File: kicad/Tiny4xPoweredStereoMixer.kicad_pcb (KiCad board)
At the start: 4 copper layers, 99.1 x 56.5 mm, 54 parts, among them J1 RCJ-2221, J2 RCJ-2221, J3 RCJ-2221, J4 RCJ-2221, J5 RCJ-2221, J6 PowerConnector, J7 PowerConnector, J8 PowerConnector, U1 TL072, U2 TL072, U3 TL072, U4 TL072, U5 TL072, U6 LM2611AMF/NOPB

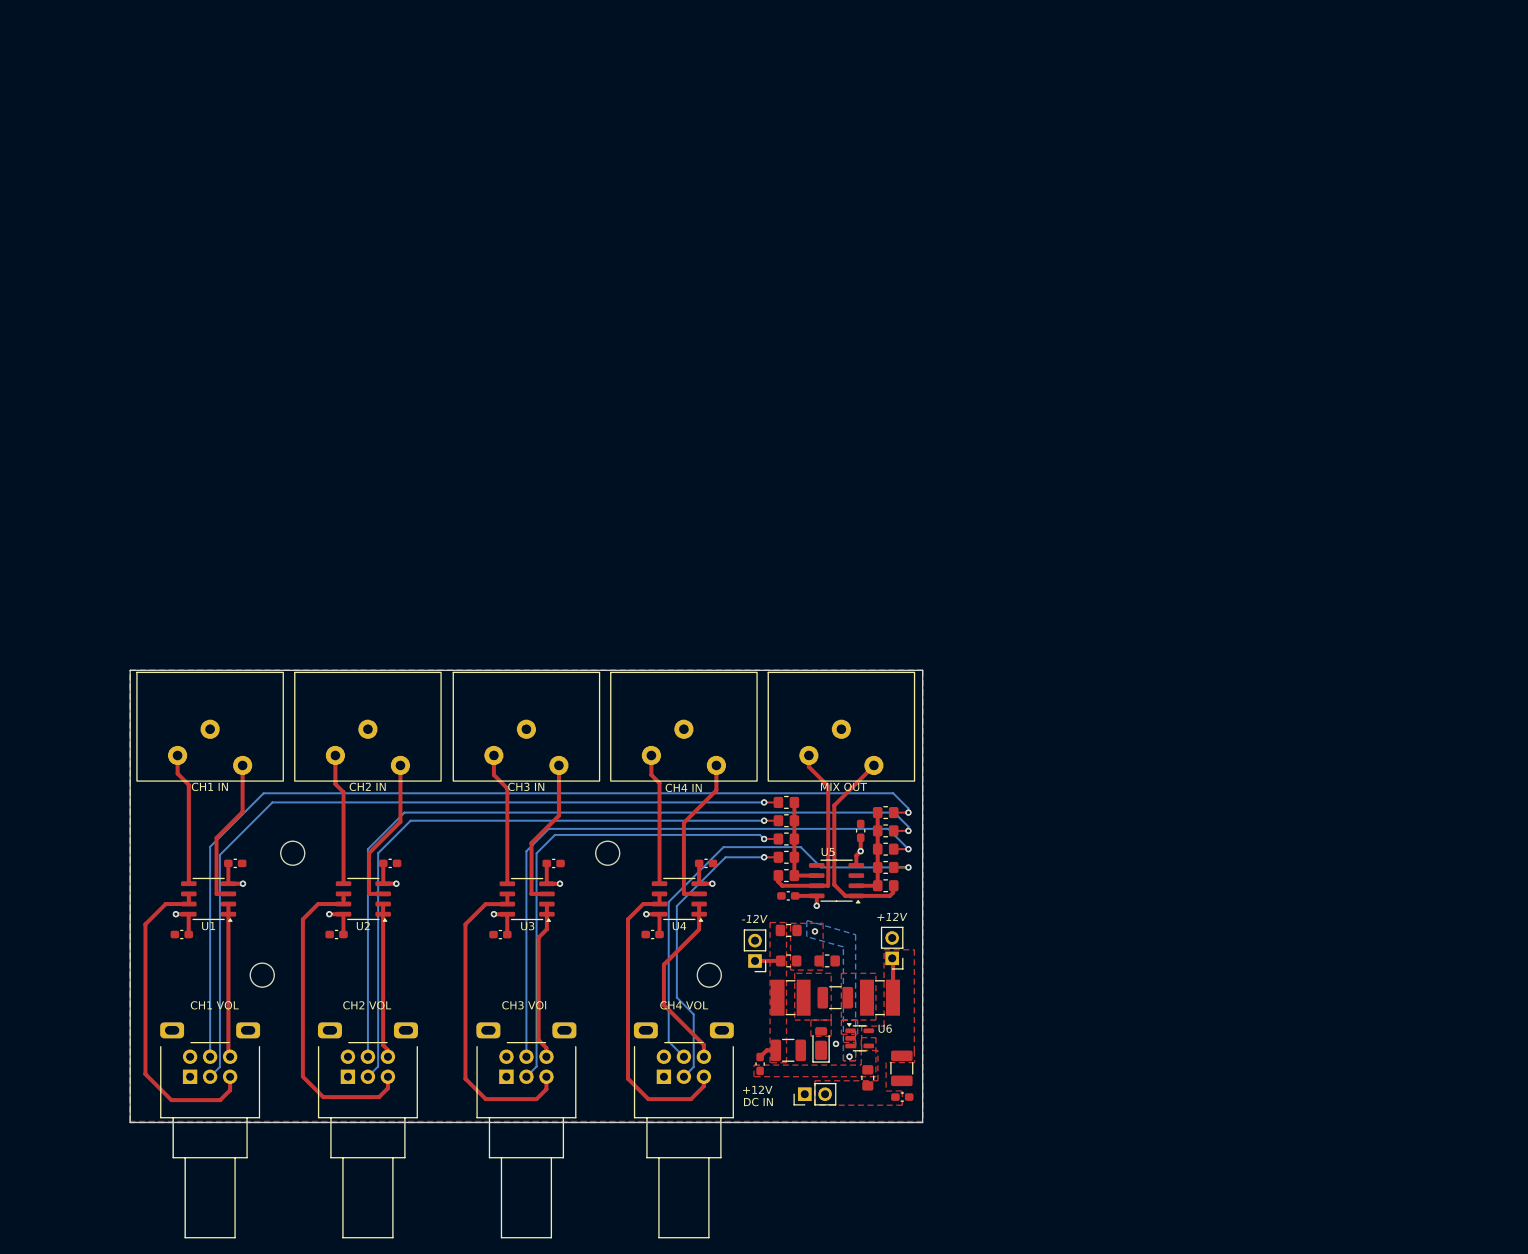
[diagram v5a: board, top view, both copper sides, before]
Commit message: - updated pots to rk12l12
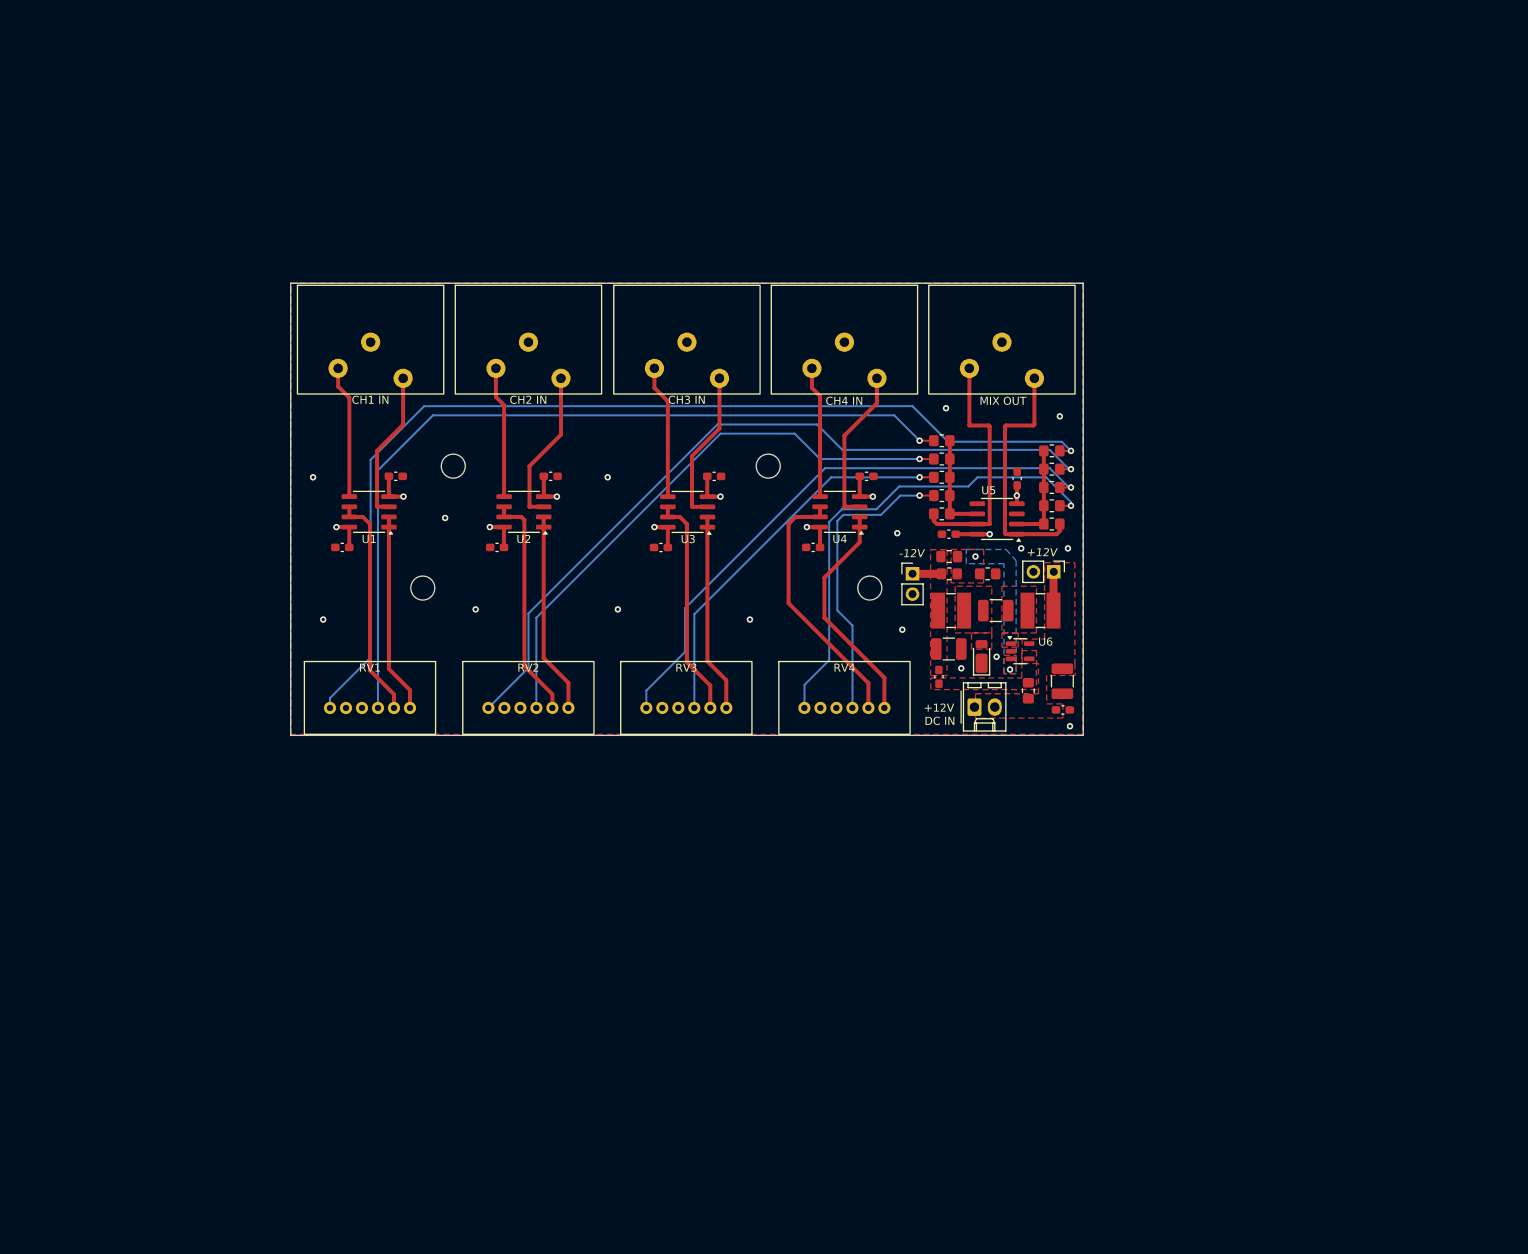
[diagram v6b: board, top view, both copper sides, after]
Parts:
- J6: footprint Connector_PinHeader_2.54mm:PinHeader_1x02_P2.54mm_Vertical -> Connector_Molex:Molex_KK-254_AE-6410-02A_1x02_P2.54mm_Vertical
- RV1, RV2, RV3, RV4: footprint Potentiometers:Potentiometer_Alps_RK09L_Double_Horizontal -> Potentiometers:Alps_RK12L12_Double_Horizontal
- moved RV4 54.3 mm to (173.1, 100.5), turned to 0 degrees
- moved RV2 54.3 mm to (133.6, 100.5), turned to 0 degrees
- moved RV3 54.3 mm to (153.3, 100.5), turned to 0 degrees
- moved RV1 54.3 mm to (113.8, 100.5), turned to 0 degrees
- moved C4 54.0 mm to (186.1, 96.4)
- moved C16 53.3 mm to (184.9, 99.9)
- moved J6 52.8 mm to (189.4, 103.7), turned to 0 degrees
- moved C11 52.4 mm to (150.2, 83.7)
- moved C13 52.4 mm to (169.2, 83.7)
- moved C5 52.4 mm to (129.7, 83.7)
- moved U6 52.4 mm to (195.1, 96.7)
- moved C7 52.4 mm to (110.3, 83.7)
- moved C1 52.4 mm to (200.3, 100.4)
- moved C12 52.4 mm to (156.8, 74.8)
- moved C14 52.4 mm to (175.9, 74.8)
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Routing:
- net Net-(U1B--): track 40.6 -> 28.4 mm
- net Net-(U3B--): track 40.1 -> 28.2 mm
- net Net-(U2B--): track 40.4 -> 28.9 mm
- net /ch3_right_mix_in: track 59.8 -> 48.7 mm
- net /ch2_right_mix_in: track 80.2 -> 71.8 mm
- net /ch1_left_mix_in: track 119.4 -> 127.2 mm
- net Net-(U4A--): track 23.0 -> 28.8 mm
- net Net-(U2A--): track 19.3 -> 25.2 mm
- net Net-(U1A--): track 19.2 -> 25.0 mm
- net Net-(U4B--): track 38.3 -> 32.7 mm
- net Net-(J5-Pin_2): track 24.5 -> 30.0 mm
- net /ch3_left_mix_in: track 77.5 -> 72.4 mm
- net Net-(J5-Pin_3): track 26.0 -> 30.9 mm
- net Net-(U3A--): track 19.9 -> 24.8 mm
- net /ch4_left_mix_in: track 55.8 -> 60.2 mm
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
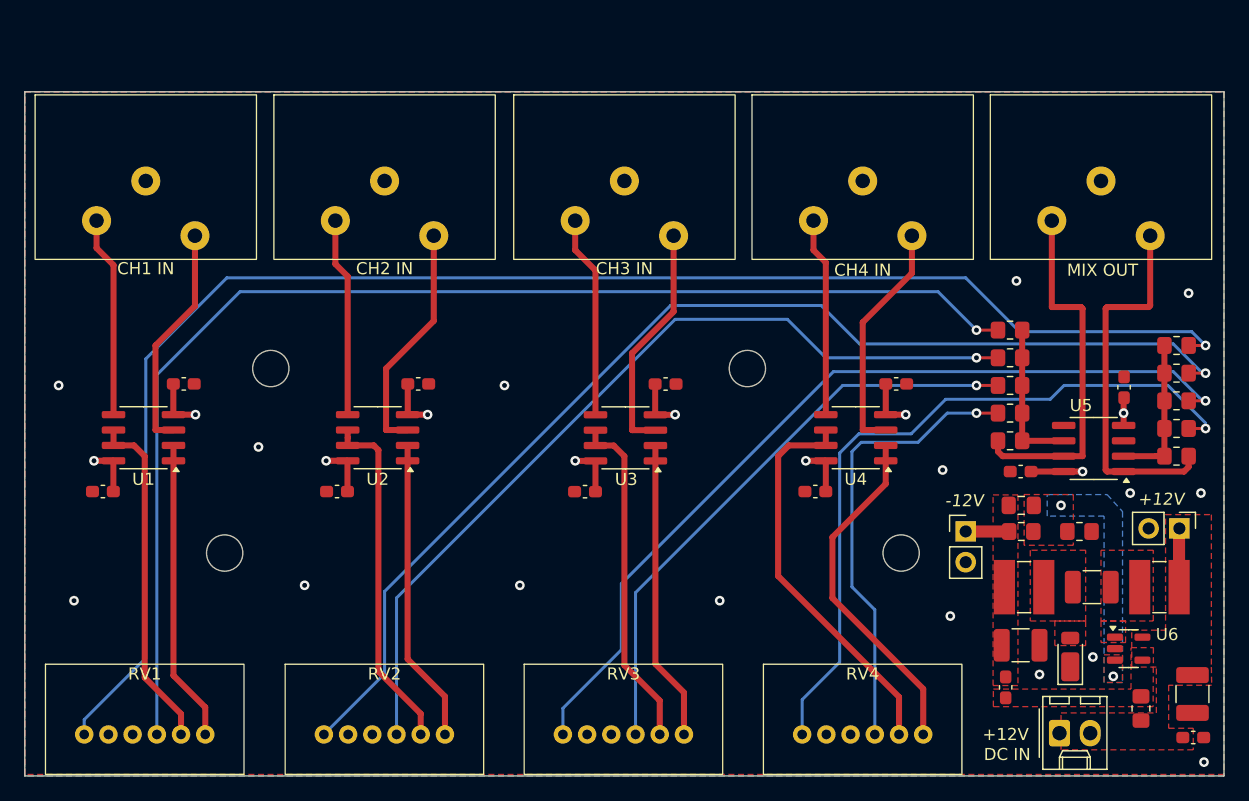
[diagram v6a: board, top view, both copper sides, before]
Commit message: replaced phono connectors with 3.5mm stereo jack connectors so that unplugged connections are switched to ground
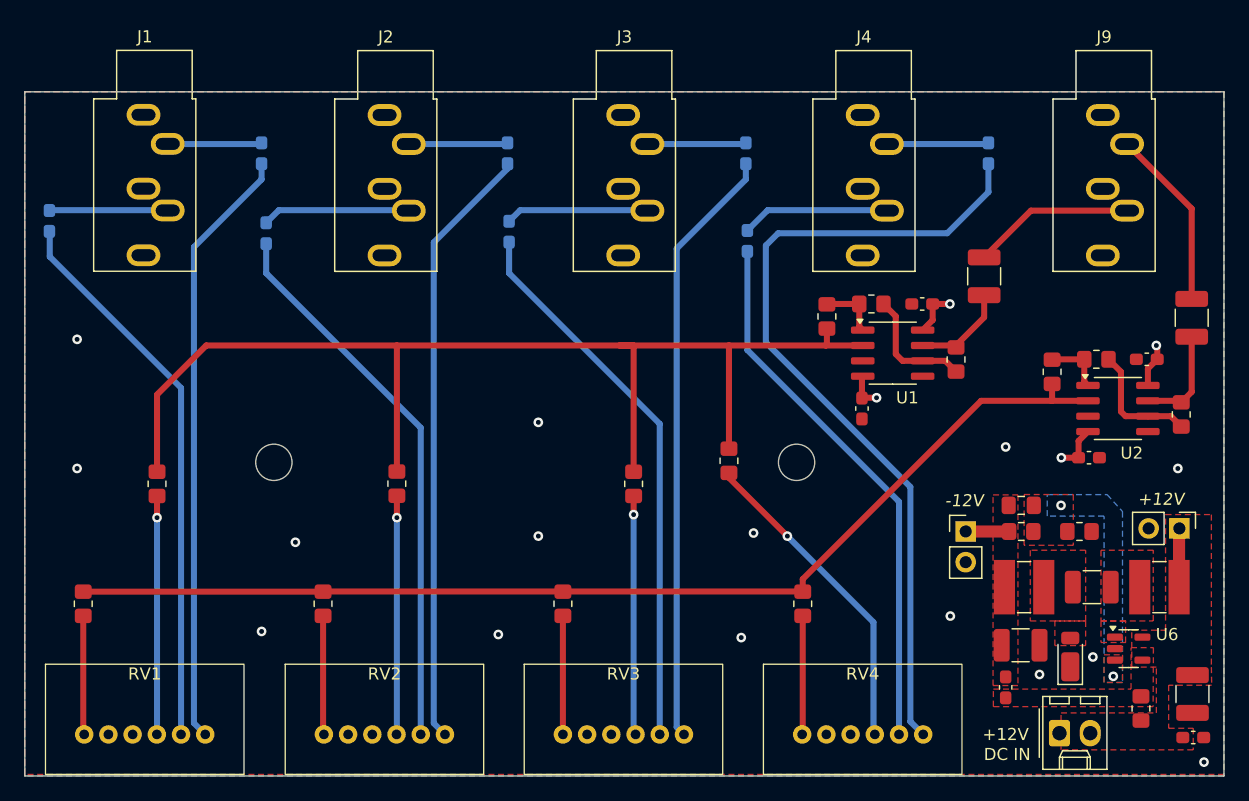
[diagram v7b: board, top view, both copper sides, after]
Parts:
- removed H3, H4: MountingHole, MountingHole:MountingHole_3mm
- removed J5: RCJ-2221, RCAJack:CUI_DEVICES_RCJ-2211
- removed U3, U4, U5: TL072, Package_SO:SOIC-8_3.9x4.9mm_P1.27mm
- added C17: 100nF, Capacitor_SMD:C_0603_1608Metric_Pad1.08x0.95mm_HandSolder, B.Cu at (183.5, 55.8)
- added C18: 100nF, Capacitor_SMD:C_0603_1608Metric_Pad1.08x0.95mm_HandSolder, B.Cu at (163.6, 63.0)
- added C19: 10uF, Capacitor_SMD:C_1210_3225Metric_Pad1.33x2.70mm_HandSolder, F.Cu at (200.3, 69.3)
- added C20: 10uF, Capacitor_SMD:C_1210_3225Metric_Pad1.33x2.70mm_HandSolder, F.Cu at (183.1, 65.9)
- added J9: AudioJack3_SwitchTR, Connector_Audio:Jack_3.5mm_CUI_SJ1-3535NG_Horizontal, F.Cu at (192.9, 52.6)
- added R12: 10k, Resistor_SMD:R_0805_2012Metric_Pad1.20x1.40mm_HandSolder, F.Cu at (173.8, 68.2)
- added R13: 10k, Resistor_SMD:R_0805_2012Metric_Pad1.20x1.40mm_HandSolder, F.Cu at (188.7, 73.8)
- added R14: 10k, Resistor_SMD:R_0805_2012Metric_Pad1.20x1.40mm_HandSolder, F.Cu at (192.4, 72.8)
- added R15: 10k, Resistor_SMD:R_0805_2012Metric_Pad1.20x1.40mm_HandSolder, F.Cu at (199.4, 77.3)
- C10, C11, C12, C14, C5, C7: moved to B.Cu
- J1, J2, J3, J4: value RCJ-2221 -> AudioJack3_SwitchTR; footprint RCAJack:CUI_DEVICES_RCJ-2211 -> Connector_Audio:Jack_3.5mm_CUI_SJ1-3535NG_Horizontal
- moved R4 92.8 mm to (108.7, 93.0), turned to 90 degrees
- moved C8 75.0 mm to (191.8, 80.9)
- moved R3 73.0 mm to (128.5, 93.0), turned to 90 degrees
- moved R8 71.6 mm to (114.8, 83.1), turned to 90 degrees
- moved U1 62.3 mm to (175.6, 72.3), turned to 0 degrees
- moved U2 61.2 mm to (194.2, 76.8), turned to 0 degrees
- moved C10 54.5 mm to (143.8, 55.8), turned to -90 degrees
- moved R2 53.4 mm to (148.3, 93.0), turned to 90 degrees
- moved H1 52.4 mm to (124.5, 81.3)
- moved R7 51.7 mm to (134.6, 83.0), turned to 90 degrees
- moved H2 47.8 mm to (167.6, 81.3)
- moved C6 36.7 mm to (173.0, 76.8), turned to -90 degrees
- moved C14 34.4 mm to (143.9, 62.2), turned to -90 degrees
- moved R1 34.1 mm to (168.1, 93.0), turned to 90 degrees
- moved C11 33.9 mm to (123.8, 62.4), turned to -90 degrees
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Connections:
- C10 pad 1: -12V -> Net-(C10-Pad1)
- C10 pad 2: GND -> Net-(C10-Pad2)
- C11 pad 1: +12V -> Net-(C11-Pad1)
- C11 pad 2: GND -> Net-(C11-Pad2)
- C12 pad 1: -12V -> Net-(C12-Pad1)
- C12 pad 2: GND -> Net-(C12-Pad2)
- C14 pad 1: -12V -> Net-(C14-Pad1)
- C14 pad 2: GND -> Net-(C14-Pad2)
- C5 pad 1: +12V -> Net-(C5-Pad1)
- C5 pad 2: GND -> Net-(C5-Pad2)
- C7 pad 1: +12V -> Net-(C7-Pad1)
- C7 pad 2: GND -> Net-(C7-Pad2)
- R1 pad 2: Net-(U5A--) -> Net-(U2A--)
- R10 pad 1: Net-(U5B--) -> Net-(U1B--)
- R10 pad 2: Net-(J5-Pin_2) -> Net-(C20-Pad1)
- R2 pad 2: Net-(U5A--) -> Net-(U2A--)
- R3 pad 2: Net-(U5A--) -> Net-(U2A--)
- R4 pad 2: Net-(U5A--) -> Net-(U2A--)
- R5 pad 2: Net-(U5B--) -> Net-(U1A--)
- R6 pad 2: Net-(U5B--) -> Net-(U1A--)
- R7 pad 2: Net-(U5B--) -> Net-(U1A--)
- R8 pad 2: Net-(U5B--) -> Net-(U1A--)
- R9 pad 1: Net-(U5A--) -> Net-(U1A--)
- R9 pad 2: Net-(J5-Pin_3) -> Net-(R12-Pad1)
- RV1 pad 3: Net-(U1B--) -> Net-(C7-Pad2)
- RV1 pad 6: Net-(U1A--) -> Net-(C5-Pad2)
- RV2 pad 3: Net-(U2B--) -> Net-(C11-Pad2)
- RV2 pad 6: Net-(U2A--) -> Net-(C10-Pad2)
- RV3 pad 3: Net-(U3B--) -> Net-(C14-Pad2)
- RV3 pad 6: Net-(U3A--) -> Net-(C12-Pad2)
- U1 pad 1: Net-(U1A--) -> Net-(R12-Pad1)
- U1 pad 3: Net-(J1-Pin_3) -> GND
- U1 pad 5: Net-(J1-Pin_2) -> GND
- U1 pad 7: Net-(U1B--) -> Net-(C20-Pad1)
- U2 pad 1: Net-(U2A--) -> Net-(R13-Pad2)
- U2 pad 3: Net-(J2-Pin_3) -> GND
- U2 pad 5: Net-(J2-Pin_2) -> GND
- U2 pad 7: Net-(U2B--) -> Net-(C19-Pad1)
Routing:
- net /ch1_left_mix_in: track 127.2 -> 9.83 mm, vias 1 -> 0
- net /ch2_left_mix_in: track 95.2 -> 9.82 mm, vias 1 -> 0
- net /ch1_right_mix_in: track 103.3 -> 19.7 mm
- net Net-(U1A--): track 25.0 -> 98.3 mm
- net Net-(U2A--): track 25.2 -> 91.6 mm
- net /ch3_left_mix_in: track 72.4 -> 9.54 mm, vias 1 -> 0
- net /ch2_right_mix_in: track 71.8 -> 19.7 mm
- net /ch4_left_mix_in: track 60.2 -> 9.81 mm, vias 1 -> 0
- net Net-(C10-Pad2): track 0.00 -> 50.1 mm
- net Net-(C5-Pad2): track 0.00 -> 49.8 mm
- net Net-(C12-Pad2): track 0.00 -> 49.8 mm
- net Net-(C7-Pad2): track 0.00 -> 46.1 mm
- net Net-(C11-Pad2): track 0.00 -> 45.8 mm
- net Net-(C14-Pad2): track 0.00 -> 45.8 mm
- net Net-(C17-Pad2): track 28.8 -> 68.3 mm
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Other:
- board text added: "Tiny 4-Channel Active Stereo Mixer Rev${REVISION} ${ISSUE_DATE}"
- board text removed: "Tiny 4x Powered Stereo Mixer Rev${REVISION} ${ISSUE_DATE}"

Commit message: completed revb layout
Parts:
- added TP1: TestPoint, TestPoint:TestPoint_Keystone_5005-5009_Compact, F.Cu at (148.6, 82.8)
- moved R5 13.0 mm to (175.0, 81.8)
- moved C6 12.1 mm to (185.2, 77.2)
- moved R9 9.79 mm to (175.0, 77.7)
- moved C8 9.64 mm to (200.3, 76.3), turned to 90 degrees
- moved R12 8.29 mm to (177.4, 75.7), turned to 90 degrees
- moved U1 6.10 mm to (181.5, 73.9), turned to 90 degrees
- moved C19 6.10 mm to (200.4, 63.2)
- moved R15 5.03 mm to (200.2, 72.4)
- moved R10 4.62 mm to (185.4, 72.4)
- moved C13 4.58 mm to (192.2, 71.6), turned to -90 degrees
- moved R13 4.04 mm to (189.7, 77.7)
- moved C20 3.94 mm to (183.1, 62.0)
- moved U2 3.54 mm to (196.2, 73.9), turned to 90 degrees
- moved C9 3.33 mm to (177.4, 71.5), turned to -90 degrees
- moved R14 2.96 mm to (192.2, 75.7), turned to 90 degrees
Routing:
- net Net-(C17-Pad2): track 68.3 -> 53.2 mm
- net Net-(C20-Pad1): track 8.10 -> 14.3 mm
- net Net-(C19-Pad2): track 15.0 -> 8.96 mm
- net /ch4_right_mix_in: track 26.6 -> 21.3 mm
- net Net-(U1A--): track 98.3 -> 103.0 mm
- net Net-(C19-Pad1): track 8.63 -> 13.1 mm
- net GND: track 0.00 -> 2.86 mm, vias 15 -> 24
- net Net-(U2A--): track 91.6 -> 94.3 mm
- net Net-(C20-Pad2): track 13.4 -> 11.7 mm
- net Net-(U2B--): track 10.2 -> 11.5 mm
- net Net-(U1B--): track 10.1 -> 11.3 mm
